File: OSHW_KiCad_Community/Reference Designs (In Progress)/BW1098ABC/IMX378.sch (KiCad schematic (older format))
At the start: 11 parts, among them J5 24-5804-030-000-829+

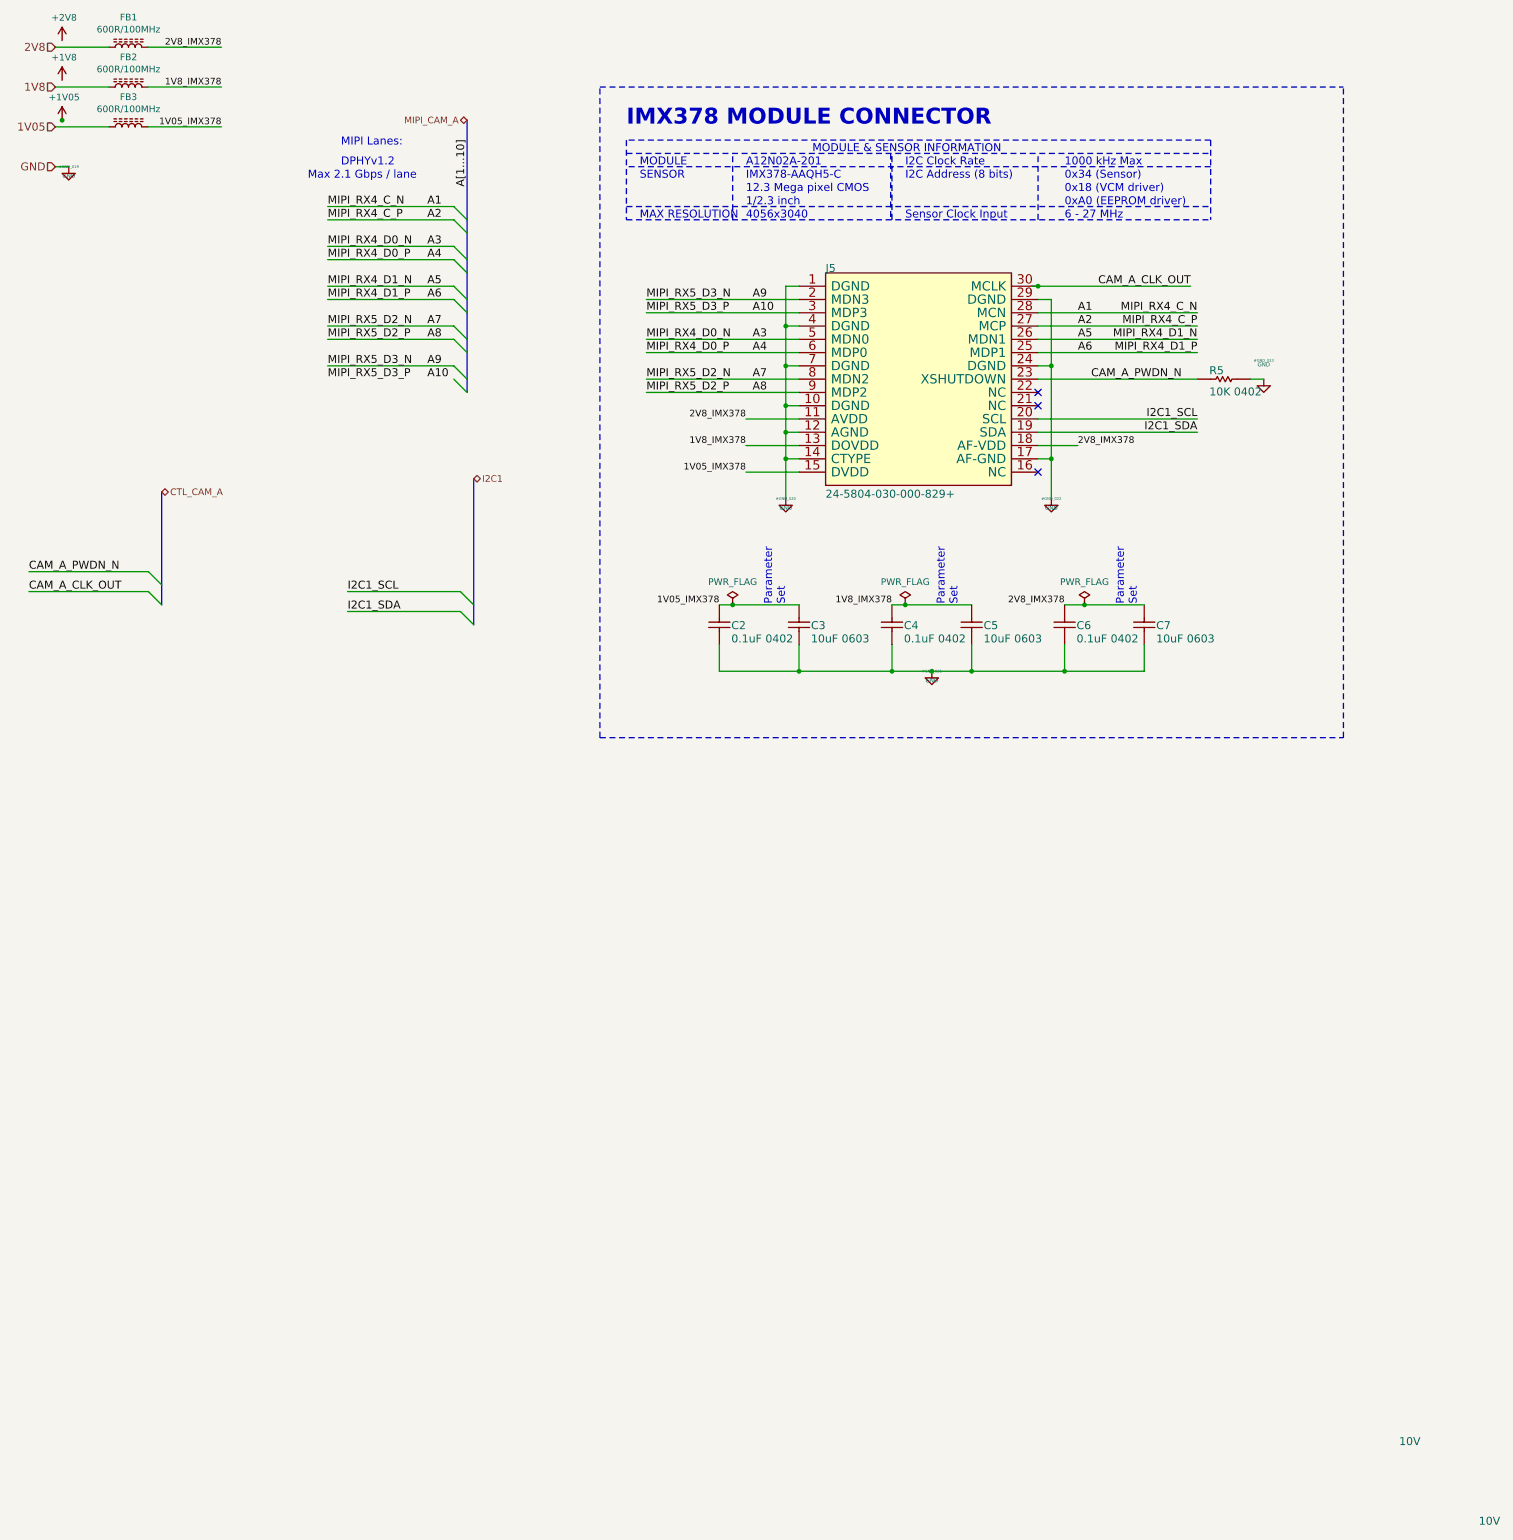
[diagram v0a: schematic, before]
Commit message: BW1098ABC - added back in usbc, got rid of hierarchical labeling in favor of globals. Passes ERC
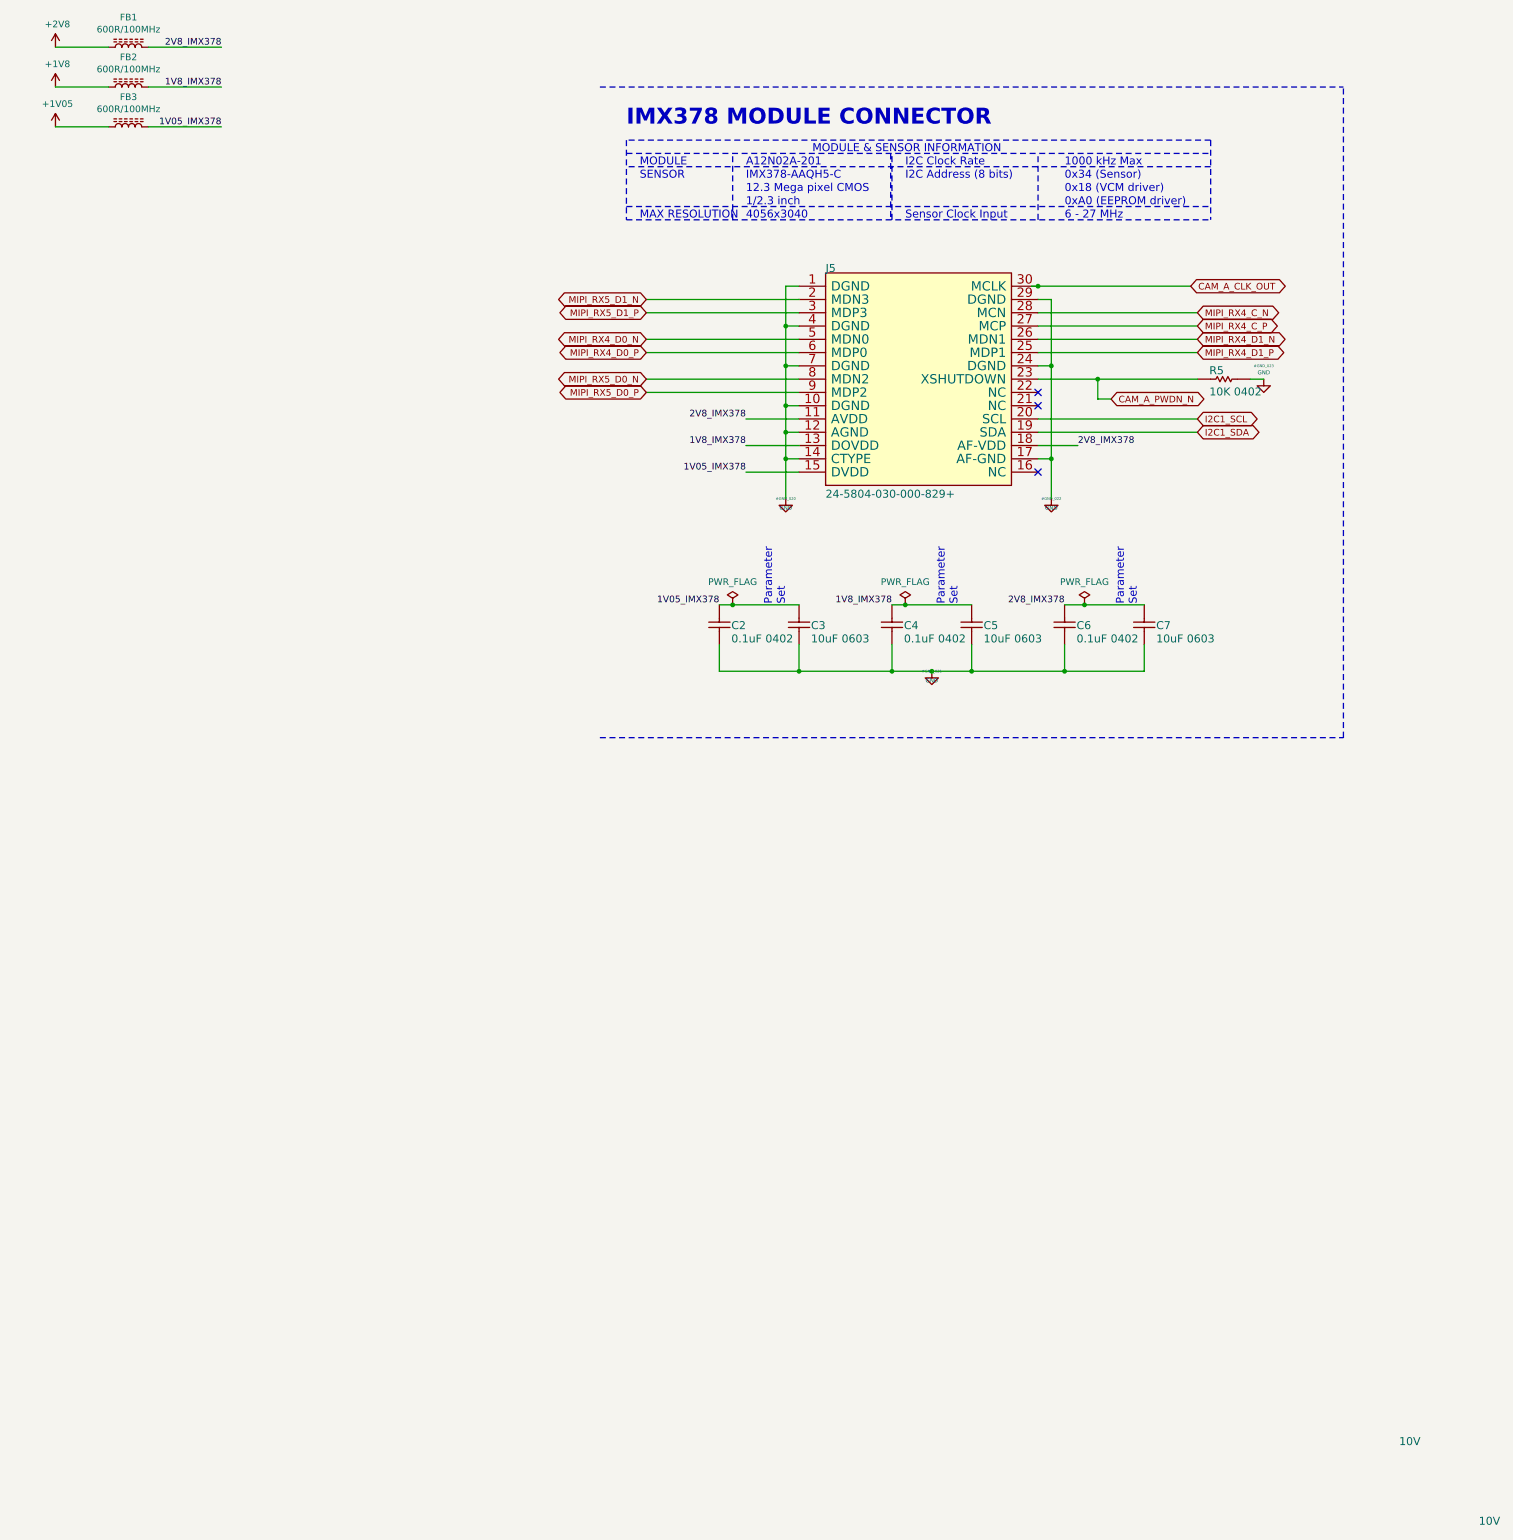
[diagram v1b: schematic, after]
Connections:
- net 1V05 is gone; now on net +1V0: FB3.1
- net 1V8 is gone; now on net +1V8: FB2.1
- net 2V8 is gone; now on net +2V8: FB1.1
- net A1 renamed MIPI_RX4_C_N
- net A10 renamed MIPI_RX5_D1_P
- net A2 renamed MIPI_RX4_C_P
- net A3 renamed MIPI_RX4_D0_N
- net A4 renamed MIPI_RX4_D0_P
- net A5 renamed MIPI_RX4_D1_N
- net A6 renamed MIPI_RX4_D1_P
- net A7 renamed MIPI_RX5_D0_N
- net A8 renamed MIPI_RX5_D0_P
- net A9 renamed MIPI_RX5_D1_N
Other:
- note removed: "DPHYv1.2"
- note removed: "MIPI Lanes:"
- note removed: "Max 2.1 Gbps / lane"

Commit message: going through footprints and datasheet stuff
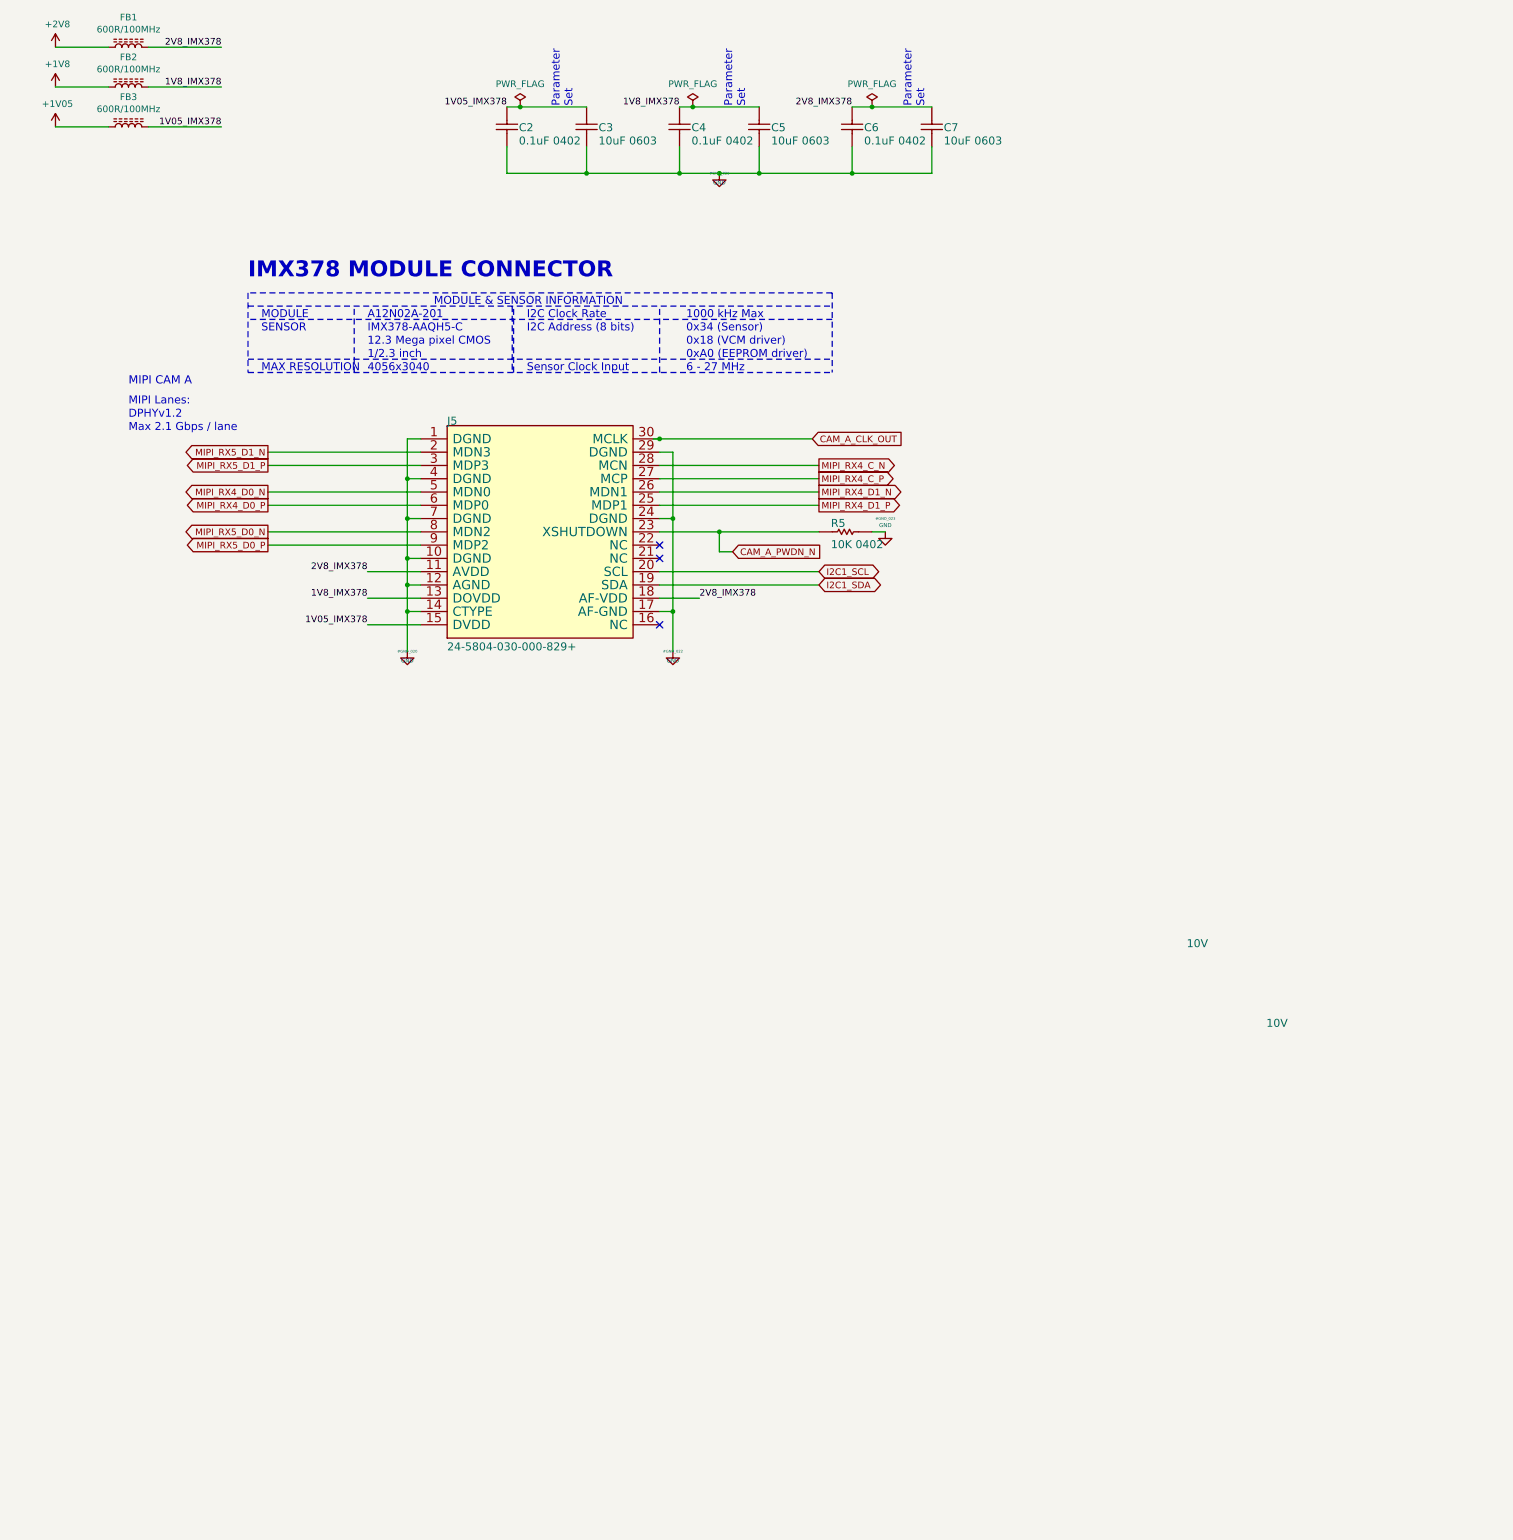
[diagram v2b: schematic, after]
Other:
- note added: "DPHYv1.2"
- note added: "MIPI CAM A"
- note added: "MIPI Lanes:"
- note added: "Max 2.1 Gbps / lane"
- moved on the sheet: C2, C3, C4, C5, C6, C7, J5, R5

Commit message: both camera connector footprints completed
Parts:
- FB1, FB2, FB3: footprint OSHW_LuxonisMaster_20201223:2508056017Y2 -> Luxonis_Kicad_Master:2508056017Y2
- J5: footprint fp_luxonis:245804030000829 -> Luxonis_Kicad_Master:A12N01A-201_IMX378
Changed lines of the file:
@@
 F 0 "FB1" V 1825 850 50  0000 C CNN
 F 1 "600R/100MHz" V 1734 850 50  0000 C CNN
-F 2 "OSHW_LuxonisMaster_20201223:2508056017Y2" H 1600 850 50  0001 C CNN
+F 2 "Luxonis_Kicad_Master:2508056017Y2" H 1600 850 50  0001 C CNN
 F 3 "~" H 1600 850 50  0001 C CNN
 	1    1600 850
@@
 F 0 "J5" H 4000 6900 60  0000 L BNN
 F 1 "24-5804-030-000-829+" H 4000 5200 60  0000 L BNN
-F 2 "fp_luxonis:245804030000829" H 4000 5200 60  0001 C CNN
+F 2 "Luxonis_Kicad_Master:A12N01A-201_IMX378" H 4000 5200 60  0001 C CNN
 F 3 "https://www.mouser.com/datasheet/2/909/5804-1525720.pdf" H 4000 5200 60  0001 C CNN
 	1    3800 5300
@@
 F 0 "FB2" V 1825 1150 50  0000 C CNN
 F 1 "600R/100MHz" V 1734 1150 50  0000 C CNN
-F 2 "OSHW_LuxonisMaster_20201223:2508056017Y2" H 1600 1150 50  0001 C CNN
+F 2 "Luxonis_Kicad_Master:2508056017Y2" H 1600 1150 50  0001 C CNN
 F 3 "~" H 1600 1150 50  0001 C CNN
 	1    1600 1150
@@
 F 0 "FB3" V 1825 1450 50  0000 C CNN
 F 1 "600R/100MHz" V 1734 1450 50  0000 C CNN
-F 2 "OSHW_LuxonisMaster_20201223:2508056017Y2" H 1600 1450 50  0001 C CNN
+F 2 "Luxonis_Kicad_Master:2508056017Y2" H 1600 1450 50  0001 C CNN
 F 3 "~" H 1600 1450 50  0001 C CNN
 	1    1600 1450
@@
 $EndComp
 $Comp
-L DEPTH:+1V05 #PWR?
+L BW1098ABC-rescue:+1V05-DEPTH #PWR?
 U 1 1 5FFCE43E
 P 1050 1450
 AR Path="/604AEAFA/5FFCE43E" Ref="#PWR?"  Part="1"
 AR Path="/5FF8D4A5/5FFCE43E" Ref="#PWR0116"  Part="1"
+AR Path="/5FFCE43E" Ref="#PWR0116"  Part="1"
 F 0 "#PWR0116" H 1050 1300 50  0001 C CNN
 F 1 "+1V05" H 1065 1623 50  0000 C CNN
